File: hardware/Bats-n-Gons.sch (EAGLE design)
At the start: 4 parts, among them X4 32.768

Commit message: replaced spaces in file names with dashes added local library for components
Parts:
- added U$2: (no value), SophiEaglev9:USB_MICRO_LEGS
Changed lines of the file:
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@@
 <layer number="132" name="bAdjust" color="7" fill="1" visible="no" active="no"/>
 <layer number="133" name="bottom_silk" color="7" fill="1" visible="yes" active="yes"/>
+<layer number="134" name="silk_top" color="7" fill="1" visible="no" active="no"/>
+<layer number="135" name="silk_bottom" color="7" fill="1" visible="no" active="no"/>
+<layer number="136" name="silktop" color="7" fill="1" visible="yes" active="yes"/>
+<layer number="137" name="silkbottom" color="7" fill="1" visible="yes" active="yes"/>
 <layer number="144" name="Drill_legend" color="7" fill="1" visible="yes" active="yes"/>
+<layer number="145" name="DrillLegend_01-16" color="7" fill="1" visible="yes" active="yes"/>
+<layer number="146" name="DrillLegend_01-20" color="7" fill="1" visible="yes" active="yes"/>
 <layer number="150" name="Notes" color="7" fill="1" visible="no" active="no"/>
 <layer number="151" name="HeatSink" color="7" fill="1" visible="no" active="yes"/>
@@
 <layer number="154" name="FabDoc2" color="2" fill="1" visible="no" active="no"/>
 <layer number="155" name="FabDoc3" color="7" fill="15" visible="no" active="no"/>
+<layer number="166" name="AntennaArea" color="7" fill="1" visible="yes" active="yes"/>
+<layer number="168" name="4mmHeightArea" color="7" fill="1" visible="yes" active="yes"/>
 <layer number="199" name="Contour" color="7" fill="1" visible="no" active="no"/>
 <layer number="200" name="200bmp" color="1" fill="10" visible="no" active="no"/>
@@
 <part name="FRAME1" library="frames" library_urn="urn:adsk.eagle:library:229" deviceset="FRAME_B_L" device=""/>
 <part name="FRAME2" library="frames" library_urn="urn:adsk.eagle:library:229" deviceset="FRAME_B_L" device=""/>
+<part name="U$2" library="SophiEaglev9" deviceset="USB_MICRO_LEGS" device=""/>
 </parts>
 <sheets>
@@
 <attribute name="DRAWING_NAME" x="342.9" y="19.05" size="2.54" layer="94"/>
 </instance>
+<instance part="U$2" gate="G$1" x="218.44" y="228.6" smashed="yes">
+<attribute name="VALUE" x="215.9" y="220.726" size="1.778" layer="96" font="vector" align="top-left"/>
+<attribute name="NAME" x="215.9" y="236.22" size="1.778" layer="95" font="vector"/>
+</instance>
 </instances>

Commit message: continued work on prototype board design
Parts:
- added C1, C2: (no value), yapo:C0603
- added IC1: (no value), yapo:AZ1117E
- added J1: (no value), yapo:HEADER_4PIN
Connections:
- new net +3.3V: C2.P$2, IC1.OUT
- new net +5V: C1.P$2, IC1.IN, J1.1, U$2.VBUS
- net D+: now also U$2.D+
- net D-: now also U$2.D-
- net GND: now also C1.P$1, C2.P$1, IC1.GND, J1.4, U$2.GND
- net UART1_RX: now also J1.2
- net UART1_TX: now also J1.3
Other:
- moved on the sheet: U$2
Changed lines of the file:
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@@
 <part name="FRAME2" library="frames" library_urn="urn:adsk.eagle:library:229" deviceset="FRAME_B_L" device=""/>
 <part name="U$2" library="SophiEaglev9" deviceset="USB_MICRO_LEGS" device=""/>
+<part name="U$3" library="yapo" deviceset="GND" device=""/>
+<part name="IC1" library="yapo" deviceset="AZ1117E" device=""/>
+<part name="C1" library="yapo" deviceset="C" device="0603"/>
+<part name="C2" library="yapo" deviceset="C" device="0603"/>
+<part name="U$4" library="yapo" deviceset="GND" device=""/>
+<part name="U$6" library="yapo" deviceset="GND" device=""/>
+<part name="U$7" library="yapo" deviceset="GND" device=""/>
+<part name="U$8" library="yapo" deviceset="+3.3V" device=""/>
+<part name="J1" library="yapo" deviceset="HEADER_4PIN" device=""/>
+<part name="U$9" library="yapo" deviceset="+5V" device=""/>
+<part name="U$11" library="yapo" deviceset="+5V" device=""/>
+<part name="U$12" library="yapo" deviceset="+5V" device=""/>
+<part name="U$13" library="yapo" deviceset="GND" device=""/>
 </parts>
 <sheets>
@@
 <attribute name="DRAWING_NAME" x="342.9" y="19.05" size="2.54" layer="94"/>
 </instance>
-<instance part="U$2" gate="G$1" x="218.44" y="228.6" smashed="yes">
-<attribute name="VALUE" x="215.9" y="220.726" size="1.778" layer="96" font="vector" align="top-left"/>
-<attribute name="NAME" x="215.9" y="236.22" size="1.778" layer="95" font="vector"/>
-</instance>
+<instance part="U$2" gate="G$1" x="210.82" y="208.28" smashed="yes">
+<attribute name="VALUE" x="208.28" y="200.406" size="1.778" layer="96" font="vector" align="top-left"/>
+<attribute name="NAME" x="208.28" y="215.9" size="1.778" layer="95" font="vector"/>
+</instance>
+<instance part="U$3" gate="G$1" x="203.2" y="198.12" smashed="yes"/>
+<instance part="IC1" gate="G$1" x="254" y="175.26" smashed="yes">
+<attribute name="NAME" x="261.62" y="185.42" size="1.27" layer="95"/>
+<attribute name="VALUE" x="261.62" y="182.88" size="1.27" layer="96"/>
+</instance>
+<instance part="C1" gate="G$1" x="233.68" y="160.02" smashed="yes">
+<attribute name="NAME" x="236.22" y="165.1" size="1.778" layer="95" font="vector"/>
+<attribute name="VALUE" x="236.22" y="162.56" size="1.778" layer="96" font="vector"/>
+</instance>
+<instance part="C2" gate="G$1" x="271.78" y="160.02" smashed="yes">
+<attribute name="NAME" x="274.32" y="165.1" size="1.778" layer="95" font="vector"/>
+<attribute name="VALUE" x="274.32" y="162.56" size="1.778" layer="96" font="vector"/>
+</instance>
+<instance part="U$4" gate="G$1" x="233.68" y="152.4" smashed="yes"/>
+<instance part="U$6" gate="G$1" x="254" y="152.4" smashed="yes"/>
+<instance part="U$7" gate="G$1" x="271.78" y="152.4" smashed="yes"/>
+<instance part="U$8" gate="G$1" x="271.78" y="185.42" smashed="yes">
+<attribute name="VALUE" x="273.05" y="187.96" size="1.27" layer="96"/>
+</instance>
+<instance part="J1" gate="G$1" x="309.88" y="213.36" smashed="yes"/>
+<instance part="U$9" gate="G$1" x="233.68" y="187.96" smashed="yes">
+<attribute name="VALUE" x="234.95" y="187.96" size="1.27" layer="96"/>
+</instance>
+<instance part="U$11" gate="G$1" x="203.2" y="223.52" smashed="yes">
+<attribute name="VALUE" x="204.47" y="223.52" size="1.27" layer="96"/>
+</instance>
+<instance part="U$12" gate="G$1" x="294.64" y="231.14" smashed="yes">
+<attribute name="VALUE" x="295.91" y="231.14" size="1.27" layer="96"/>
+</instance>
+<instance part="U$13" gate="G$1" x="294.64" y="200.66" smashed="yes"/>
 </instances>
 <busses>
@@
 <pinref part="U$10" gate="G$1" pin="GND"/>
 </segment>
+<segment>
+<pinref part="U$2" gate="G$1" pin="GND"/>
+<pinref part="U$3" gate="G$1" pin="GND"/>
+<wire x1="205.74" y1="203.2" x2="203.2" y2="203.2" width="0.1524" layer="91"/>
+<wire x1="203.2" y1="203.2" x2="203.2" y2="198.12" width="0.1524" layer="91"/>
+</segment>
+<segment>
+<pinref part="C1" gate="G$1" pin="P$1"/>
+<pinref part="U$4" gate="G$1" pin="GND"/>
+<wire x1="233.68" y1="154.94" x2="233.68" y2="152.4" width="0.1524" layer="91"/>
+</segment>
+<segment>
+<pinref part="U$6" gate="G$1" pin="GND"/>
+<pinref part="IC1" gate="G$1" pin="GND"/>
+<wire x1="254" y1="152.4" x2="254" y2="162.56" width="0.1524" layer="91"/>
+</segment>
+<segment>
+<pinref part="C2" gate="G$1" pin="P$1"/>
+<pinref part="U$7" gate="G$1" pin="GND"/>
+<wire x1="271.78" y1="154.94" x2="271.78" y2="152.4" width="0.1524" layer="91"/>
+</segment>
+<segment>
+<pinref part="J1" gate="G$1" pin="4"/>
+<pinref part="U$13" gate="G$1" pin="GND"/>
+<wire x1="302.26" y1="205.74" x2="294.64" y2="205.74" width="0.1524" layer="91"/>
+<wire x1="294.64" y1="205.74" x2="294.64" y2="200.66" width="0.1524" layer="91"/>
+</segment>
 </net>
 <net name="AREF" class="4">
@@
 <label x="20.32" y="35.56" size="1.778" layer="95"/>
 <pinref part="U$1" gate="G$4" pin="PD09/I4/SERCOM7.1+6.0/TCC0.2"/>
-</segment>
-</net>
-<net name="D-" class="1">
-<segment>
-<wire x1="154.94" y1="210.82" x2="162.56" y2="210.82" width="0.1524" layer="91"/>
-<label x="160.02" y="210.82" size="1.778" layer="95"/>
-<pinref part="U$1" gate="G$1" pin="PA24/I8/SERCOM3+5.2/D-"/>
-</segment>
-</net>
-<net name="D+" class="1">
-<segment>
-<wire x1="154.94" y1="208.28" x2="162.56" y2="208.28" width="0.1524" layer="91"/>
-<label x="160.02" y="208.28" size="1.778" layer="95"/>
-<pinref part="U$1" gate="G$1" pin="PA25/19/SERCOM3+5.3/D+"/>
 </segment>
 </net>
@@
 <label x="17.78" y="144.78" size="1.778" layer="95"/>
 </segment>
+<segment>
+<pinref part="J1" gate="G$1" pin="3"/>
+<wire x1="302.26" y1="210.82" x2="287.02" y2="210.82" width="0.1524" layer="91"/>
+<label x="287.02" y="210.82" size="1.778" layer="95"/>
+</segment>
 </net>
 <net name="UART1_RX" class="0">
@@
 <label x="17.78" y="142.24" size="1.778" layer="95"/>
 </segment>
+<segment>
+<pinref part="J1" gate="G$1" pin="2"/>
+<wire x1="302.26" y1="215.9" x2="287.02" y2="215.9" width="0.1524" layer="91"/>
+<label x="287.02" y="215.9" size="1.778" layer="95"/>
+</segment>
 </net>
 <net name="UART2_RX" class="0">
@@
 </segment>
 </net>
+<net name="D-" class="0">
+<segment>
+<pinref part="U$1" gate="G$1" pin="PA24/I8/SERCOM3+5.2/D-"/>
+<wire x1="154.94" y1="210.82" x2="180.34" y2="210.82" width="0.1524" layer="91"/>
+<label x="177.8" y="210.82" size="1.778" layer="95"/>
+</segment>
+<segment>
+<pinref part="U$2" gate="G$1" pin="D-"/>
+<wire x1="205.74" y1="210.82" x2="195.58" y2="210.82" width="0.1524" layer="91"/>
+<label x="195.58" y="210.82" size="1.778" layer="95"/>
+</segment>
+</net>
+<net name="D+" class="0">
+<segment>
+<pinref part="U$1" gate="G$1" pin="PA25/19/SERCOM3+5.3/D+"/>
+<wire x1="154.94" y1="208.28" x2="180.34" y2="208.28" width="0.1524" layer="91"/>
+<label x="177.8" y="208.28" size="1.778" layer="95"/>
+</segment>
+<segment>
+<pinref part="U$2" gate="G$1" pin="D+"/>
+<wire x1="205.74" y1="208.28" x2="195.58" y2="208.28" width="0.1524" layer="91"/>
+<label x="195.58" y="208.28" size="1.778" layer="95"/>
+</segment>
+</net>
+<net name="+3.3V" class="0">
+<segment>
+<pinref part="C2" gate="G$1" pin="P$2"/>
+<pinref part="IC1" gate="G$1" pin="OUT"/>
+<wire x1="271.78" y1="165.1" x2="271.78" y2="175.26" width="0.1524" layer="91"/>
+<pinref part="U$8" gate="G$1" pin="+3.3V"/>
+<wire x1="269.24" y1="175.26" x2="266.7" y2="175.26" width="0.1524" layer="91"/>
+<wire x1="271.78" y1="185.42" x2="271.78" y2="175.26" width="0.1524" layer="91"/>
+<wire x1="271.78" y1="175.26" x2="269.24" y2="175.26" width="0.1524" layer="91"/>
+<junction x="271.78" y="175.26"/>
+</segment>
+</net>
+<net name="+5V" class="0">
+<segment>
+<pinref part="U$2" gate="G$1" pin="VBUS"/>
+<pinref part="U$11" gate="G$1" pin="+5V"/>
+<wire x1="205.74" y1="213.36" x2="203.2" y2="213.36" width="0.1524" layer="91"/>
+<wire x1="203.2" y1="213.36" x2="203.2" y2="220.98" width="0.1524" layer="91"/>
+</segment>
+<segment>
+<pinref part="IC1" gate="G$1" pin="IN"/>
+<wire x1="241.3" y1="175.26" x2="233.68" y2="175.26" width="0.1524" layer="91"/>
+<pinref part="C1" gate="G$1" pin="P$2"/>
+<wire x1="233.68" y1="165.1" x2="233.68" y2="175.26" width="0.1524" layer="91"/>
+<pinref part="U$9" gate="G$1" pin="+5V"/>
+<wire x1="233.68" y1="185.42" x2="233.68" y2="175.26" width="0.1524" layer="91"/>
+<junction x="233.68" y="175.26"/>
+</segment>
+<segment>
+<pinref part="J1" gate="G$1" pin="1"/>
+<pinref part="U$12" gate="G$1" pin="+5V"/>
+<wire x1="302.26" y1="220.98" x2="294.64" y2="220.98" width="0.1524" layer="91"/>
+<wire x1="294.64" y1="220.98" x2="294.64" y2="228.6" width="0.1524" layer="91"/>
+</segment>
+</net>

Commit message: checkpoint
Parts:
- added C10: NOPOP, bats-n-gons:C0603
- added C11: 100n, bats-n-gons:C0603
- added C12, C13, C14, C15, C16, C17, C18, C19, C20, C21, C22, C3, C4, C8: (no value), bats-n-gons:C0603
- added C6: 1u, bats-n-gons:C0603
- added C9: 10u, bats-n-gons:C1206
- added D13_LED, PWR_LED, RX_LED, TX_LED: (no value), bats-n-gons:LED_0603
- added IC2: IS31AP4991, bats-n-gons:IS31AP4991SOIC
- added R1, R5, R6, R7, R8: (no value), bats-n-gons:R0603
- added R2, R3: 20k, bats-n-gons:R0603
- added R4: 100, bats-n-gons:R0603
- added SPK+, SPK-: PAD100MIL, bats-n-gons:PAD100MIL
- added U$23: SMD_SWITCH, bats-n-gons:SMD_SWITCH
- C1, C2: value (none) -> 1u
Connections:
- new net N$1: C6.P$1, IC2.BYP, IC2.IN+
- new net N$10: D13_LED.A, R6.P$4
- new net N$11: R7.P$4, TX_LED.A
- new net N$13: R8.P$4, RX_LED.A
- new net N$2: C10.P$2, IC2.OUT-, R2.P$4, SPK-.P$1
- new net N$3: C10.P$1, IC2.IN-, R2.P$3, R3.P$4
- new net N$4: C11.P$2, R3.P$3
- new net N$5: IC2.OUT+, SPK+.P$1
- new net N$6: C22.P$2, R1.P$4, U$1G$5.!RESET, U$23.P$2
- new net N$7: J1.3, R4.P$4
- new net N$8: PWR_LED.A, R5.P$4
- net +3.3V: now also C12.P$2, C13.P$2, C14.P$2, C15.P$2, C16.P$2, C17.P$2, C18.P$2, C19.P$2, C20.P$2, C21.P$2, C3.P$2, C4.P$2, C8.P$2, C9.P$1, IC2.VCC, R1.P$3, R5.P$3, U$1G$5.VDDANA, U$1G$5.VDDANA1, U$1G$5.VDDANA2, U$1G$5.VDDIO, U$1G$5.VDDIO1, U$1G$5.VDDIO2, U$1G$5.VDDIO3, U$1G$5.VDDIO4, U$1G$5.VDDIO5, U$1G$5.VDDIO6, U$1G$5.VDDIO7, U$1G$5.VDDIOB, U$1G$5.VDDIOB1
- net A0: now also C11.P$1
- net D13: now also R6.P$3
- net D2: now also IC2.SDB
- net GND: now also C12.P$1, C13.P$1, C14.P$1, C15.P$1, C16.P$1, C17.P$1, C18.P$1, C19.P$1, C20.P$1, C21.P$1, C22.P$1, C3.P$1, C4.P$1, C6.P$2, C8.P$1, C9.P$2, D13_LED.C, IC2.GND, PWR_LED.C, RX_LED.C, TX_LED.C, U$1G$5.GND, U$1G$5.GND1, U$1G$5.GND2, U$1G$5.GND3, U$1G$5.GND4, U$1G$5.GND5, U$1G$5.GND6, U$1G$5.GND7, U$1G$5.GND8, U$1G$5.GND9, U$1G$5.GNDANA, U$1G$5.GNDANA1, U$1G$5.GNDIO, U$23.P$1
- net RXLED: now also R8.P$3
- net TXLED: now also R7.P$3
- net UART1_TX: now also R4.P$3; no longer J1.3

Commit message: wheeeee
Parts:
- added D1, D2: DIFFUSE, SparkFun-LED:LED-RGB-CADIFFUSE
- added D13_LED1, PWR_LED1: (no value), bats-n-gons:LED_0603
- added J2: (no value), SparkFun-Connectors:CONN_03
- added R9: 100, bats-n-gons:R0603
- renumbered IC1 to U3, IC2 to U2, R4 to R10, U$1 to U1, U$2 to USB, U$23 to SW1
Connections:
- new net N$14: J1.2, R9.P$4
- net +5V: now also J2.3
- net UART1_RX: now also R9.P$3; no longer J1.2
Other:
- moved on the sheet: D13_LED, PWR_LED, R5, R6, R7, R8, RX_LED, TX_LED

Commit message: maybe good enough for 0.0
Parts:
- removed D13_LED1, PWR_LED1: (no value), bats-n-gons:LED_0603
- removed J2: (no value), SparkFun-Connectors:CONN_03
- added C23: 0.1u, bats-n-gons:C0603
- added C24: (no value), bats-n-gons:C0603
- added L1: 10u, bats-n-gons:INDUCTOR2424
- added PAD_TOUCH, PAD_TOUCH1: PAD, bats-n-gons:PAD
- added U$1: HEADER_3PIN, bats-n-gons:HEADER_3PIN
- added U$33, U$34: PADROUND-50MIL, bats-n-gons:PADROUND-50MIL
- C21: value (none) -> 10u
- D1, D2: value DIFFUSE -> (none); device SparkFun-LED:LED-RGB-CADIFFUSE -> bats-n-gons:NEOPIXEL
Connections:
- net N$6 renamed !RESET!
- new net N$15: U$1.3, USB.VBUS
- new net N$16: J1.1, U$1.1
- new net N$17: D1.DOUT, D2.DIN
- new net N$18: C21.P$2, C23.P$2, L1.1, U1G$5.VDDCORE
- new net N$19: L1.2, U1G$5.VSW
- net +3.3V: now also C24.P$2, U$33.P$1; no longer C21.P$2
- net +5V: now also D1.VCC, D2.VCC, U$1.2, U$34.P$1; no longer J1.1, J2.3, USB.VBUS
- net A1: now also PAD_TOUCH1.P$1
- net A2: now also PAD_TOUCH.P$1
- net D2: no longer U2.SDB
- net D46: now also U2.SDB
- net GND: now also C23.P$1, C24.P$1, D1.GND, D2.GND
- net NEOPIX: now also D1.DIN
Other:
- moved on the sheet: C21

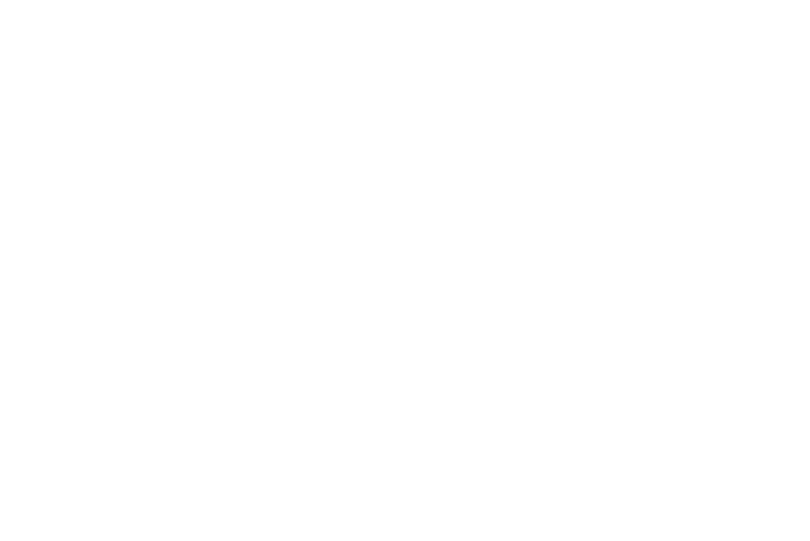
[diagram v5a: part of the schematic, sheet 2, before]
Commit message: added SWD interface so we can actually install the bootloader :-)
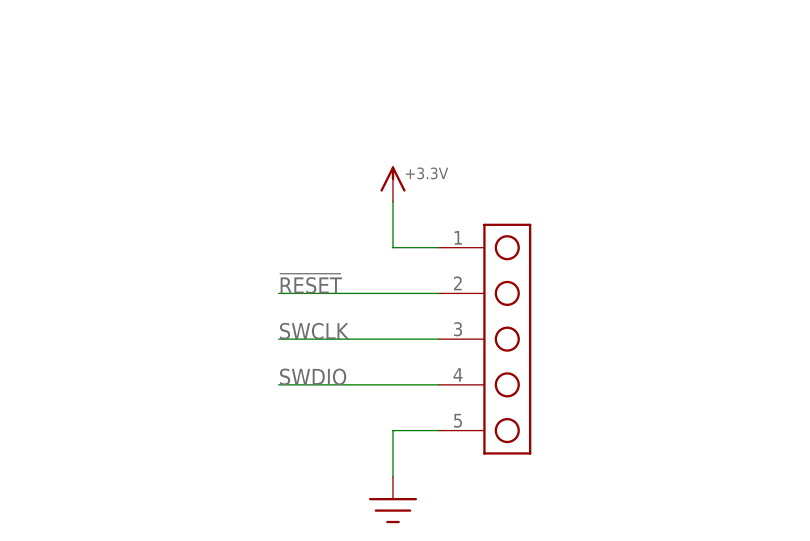
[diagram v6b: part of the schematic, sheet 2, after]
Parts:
- added J2: (no value), bats-n-gons:HEADER_5PIN
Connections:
- net !RESET!: now also J2.2
- net +3.3V: now also J2.1
- net GND: now also J2.5
- net SWCLK: now also J2.3
- net SWDIO: now also J2.4
